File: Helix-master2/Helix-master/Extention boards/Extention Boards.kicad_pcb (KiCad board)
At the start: 2 copper layers, 43.2 x 63.5 mm, 82 parts, among them J1 Conn_02x15_Odd_Even, J2 Conn_02x08_Odd_Even, U1 INA4180, U10 TPS22810, U11 INA4180, U12 LM339, U2 MC33063, U3 MCP3008, U4 TPS22810, U5 TPS22810, U6 TPS22810, U7 LM339, U8 TPS22810, U9 TPS22810

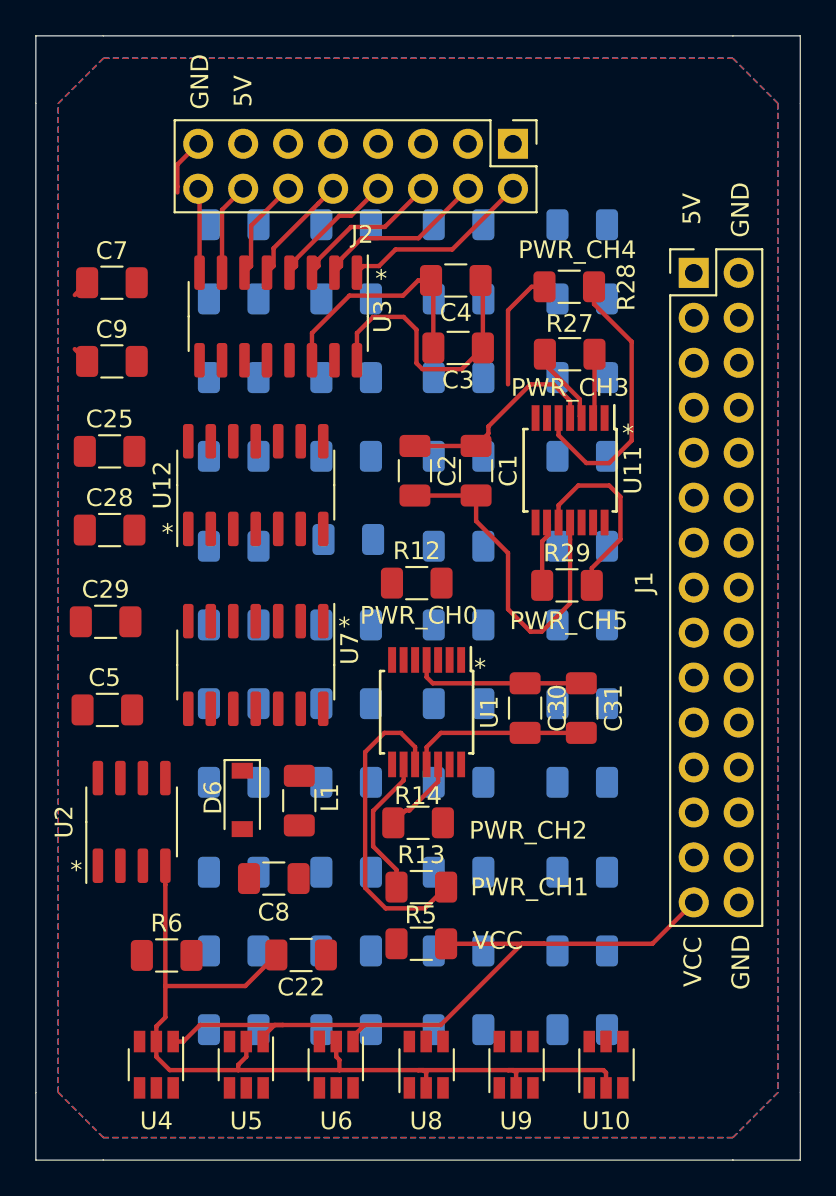
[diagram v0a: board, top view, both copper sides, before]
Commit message: Tracing and mounting holes left to do
still left to do:
M4 mounting holes.
traces for top and bottom layers
vias to connect bottom components
board silkscreen identifiers
	"Pwr_curr_sens"
	"by Chris Johnson"
	"rev 1 (mm:dd:yy)"
need to remove top 5V ground plane for Decoup. caps.
Need to write up documentation for pinout
	need to add pics of board layout to identify components

Since last commit:
removed all by pwr_curr_sens
annotated all the components
associated all the footprints
added 2 GPiO pin headers for I/O and probing.
added 5v neighboring pins for channel enable jumpers
added ground and 5V pours, bottom and top respectively.
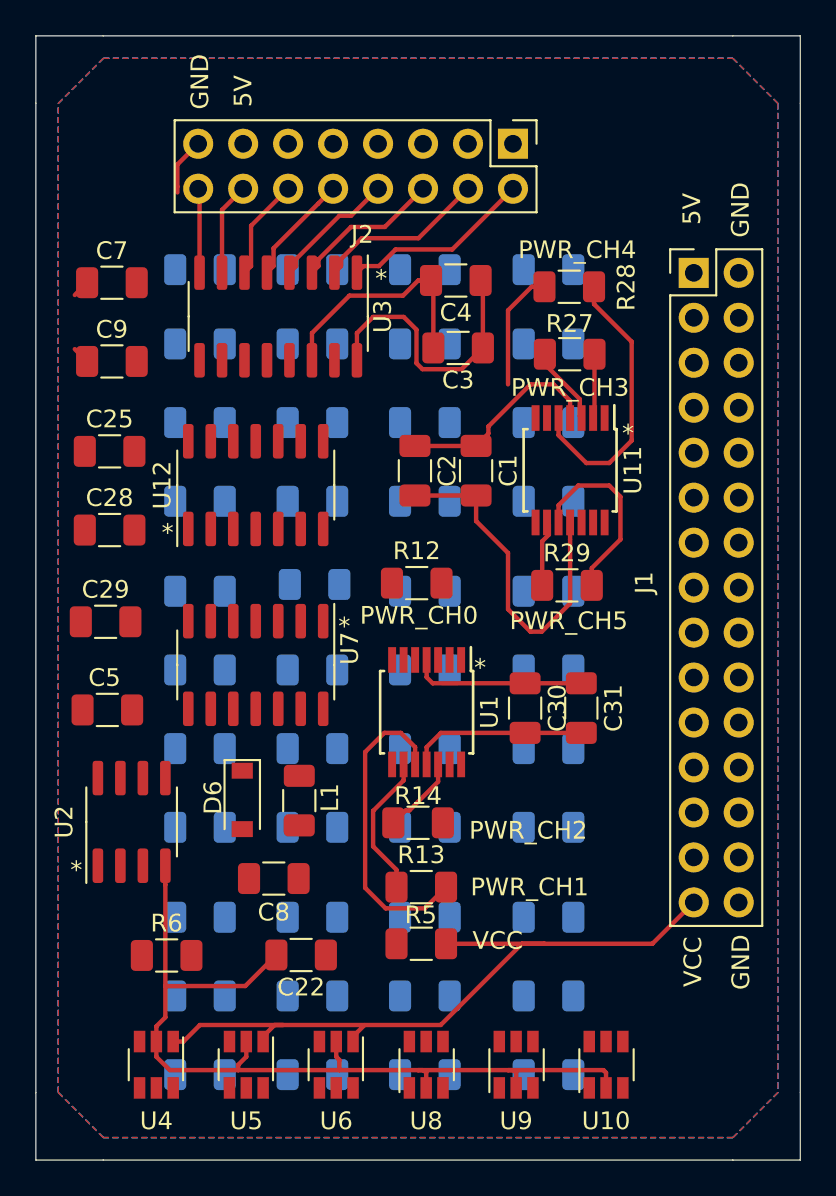
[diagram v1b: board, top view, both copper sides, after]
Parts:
- moved C11 3.18 mm to (110.9, 70.1)
- moved C12 3.18 mm to (117.2, 70.1)
- moved C13 3.18 mm to (123.6, 70.1)
- moved C17 3.18 mm to (110.9, 79.6)
- moved C18 3.18 mm to (117.2, 79.6)
- moved C19 3.18 mm to (123.6, 79.6)
- moved R15 3.18 mm to (110.9, 65.7)
- moved R16 3.18 mm to (117.2, 65.7)
- moved R17 3.18 mm to (123.6, 65.7)
- moved R3 3.18 mm to (130.6, 79.6)
- moved R7 3.18 mm to (130.6, 70.1)
- moved R8 3.18 mm to (130.6, 65.7)
- moved C20 3.18 mm to (117.2, 51.7)
- moved C21 3.18 mm to (123.6, 42.8)
- moved C23 3.18 mm to (117.2, 42.8)
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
